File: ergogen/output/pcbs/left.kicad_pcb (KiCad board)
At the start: 2 copper layers, 122 x 109.6 mm, 29 parts

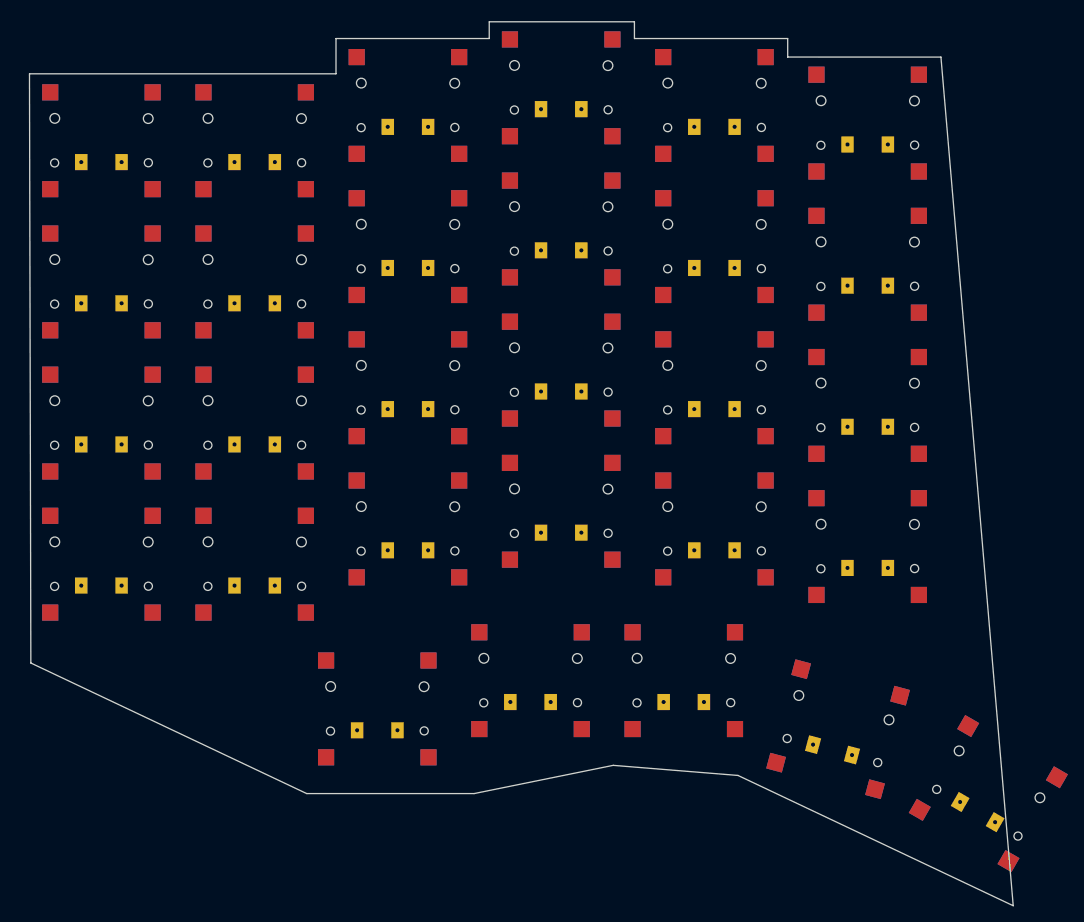
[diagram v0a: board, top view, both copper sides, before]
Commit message: feat: sane outline for left pcb
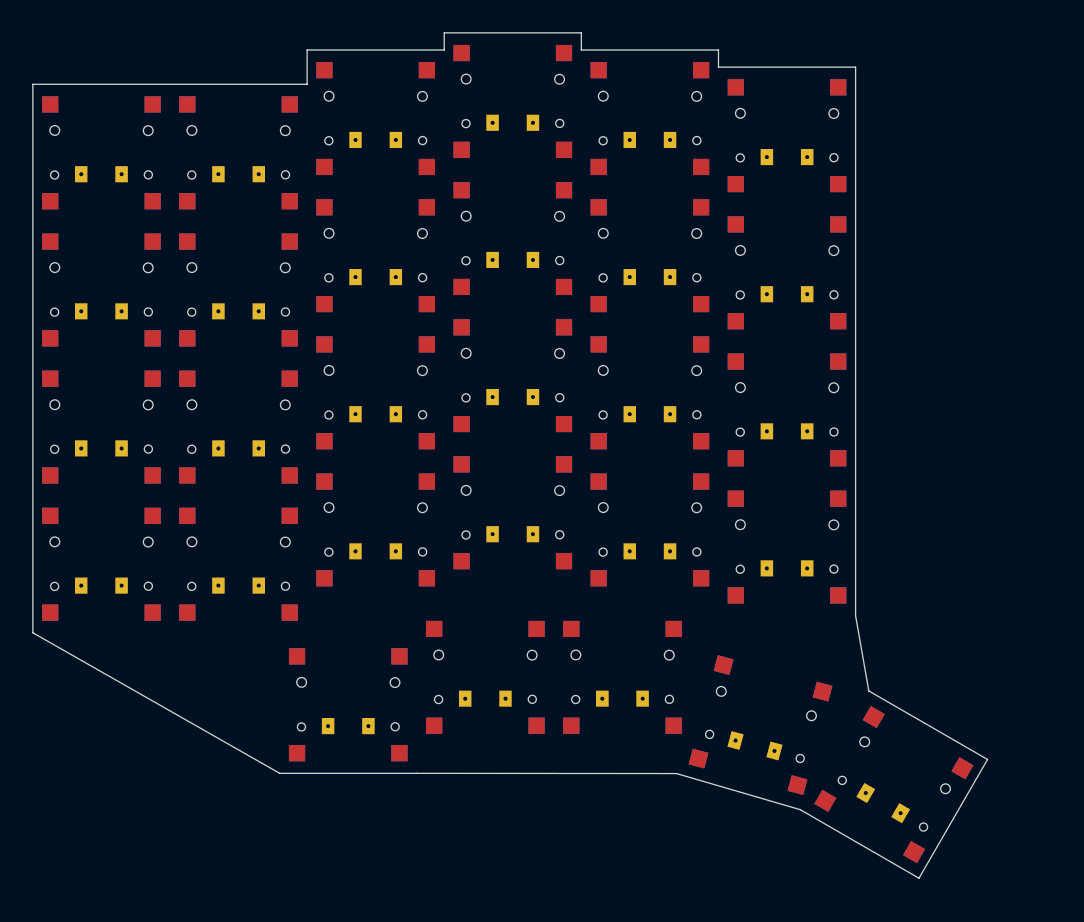
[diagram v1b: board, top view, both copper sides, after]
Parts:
- moved S29 11.8 mm to (198.2, 127.3)
- moved S24 10.1 mm to (185.0, 46.9)
- moved S23 10.1 mm to (185.0, 63.9)
- moved S22 10.0 mm to (185.0, 80.9)
- moved S21 10.0 mm to (185.0, 97.9)
- moved S28 9.63 mm to (181.7, 119.9)
- moved S20 8.16 mm to (168.0, 44.8)
- moved S19 8.08 mm to (168.0, 61.8)
- moved S18 8.02 mm to (168.0, 78.8)
- moved S17 8.00 mm to (168.0, 95.8)
- moved S27 7.61 mm to (164.6, 114.0)
- moved S16 6.23 mm to (151.0, 42.6)
- moved S15 6.12 mm to (151.0, 59.6)
- moved S14 6.04 mm to (151.0, 76.6)
- moved S13 6.00 mm to (151.0, 93.6)
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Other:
- board size 122 x 109.6 mm -> 118.4 x 104.8 mm
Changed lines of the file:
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@@
 )
 (footprint "CPG1316S01D02_reversible"
-(at 100 82.5 0)
+(at 100 83 0)
 (layer F.Cu)
 (attr smd)
@@
 )
 (footprint "CPG1316S01D02_reversible"
-(at 100 65 0)
+(at 100 66 0)
 (layer F.Cu)
 (attr smd)
@@
 )
 (footprint "CPG1316S01D02_reversible"
-(at 100 47.5 0)
+(at 100 49 0)
 (layer F.Cu)
 (attr smd)
@@
 )
 (footprint "CPG1316S01D02_reversible"
-(at 119 100 0)
+(at 117 100 0)
 (layer F.Cu)
 (attr smd)
@@
 )
 (footprint "CPG1316S01D02_reversible"
-(at 119 82.5 0)
+(at 117 83 0)
 (layer F.Cu)
 (attr smd)
@@
 )
 (footprint "CPG1316S01D02_reversible"
-(at 119 65 0)
+(at 117 66 0)
 (layer F.Cu)
 (attr smd)
@@
 )
 (footprint "CPG1316S01D02_reversible"
-(at 119 47.5 0)
+(at 117 49 0)
 (layer F.Cu)
 (attr smd)
@@
 )
 (footprint "CPG1316S01D02_reversible"
-(at 138 95.625 0)
+(at 134 95.75 0)
 (layer F.Cu)
 (attr smd)
@@
 )
 (footprint "CPG1316S01D02_reversible"
-(at 138 78.125 0)
+(at 134 78.75 0)
 (layer F.Cu)
 (attr smd)
@@
 )
 (footprint "CPG1316S01D02_reversible"
-(at 138 60.625 0)
+(at 134 61.75 0)
 (layer F.Cu)
 (attr smd)
@@
 )
 (footprint "CPG1316S01D02_reversible"
-(at 138 43.125 0)
+(at 134 44.75 0)
 (layer F.Cu)
 (attr smd)
@@
 )
 (footprint "CPG1316S01D02_reversible"
-(at 157 93.4375 0)
+(at 151 93.625 0)
 (layer F.Cu)
 (attr smd)
@@
 )
 (footprint "CPG1316S01D02_reversible"
-(at 157 75.9375 0)
+(at 151 76.625 0)
 (layer F.Cu)
 (attr smd)
@@
 )
 (footprint "CPG1316S01D02_reversible"
-(at 157 58.4375 0)
+(at 151 59.625 0)
 (layer F.Cu)
 (attr smd)
@@
 )
 (footprint "CPG1316S01D02_reversible"
-(at 157 40.9375 0)
+(at 151 42.625 0)
 (layer F.Cu)
 (attr smd)
@@
 )
 (footprint "CPG1316S01D02_reversible"
-(at 176 95.625 0)
+(at 168 95.75 0)
 (layer F.Cu)
 (attr smd)
@@
 )
 (footprint "CPG1316S01D02_reversible"
-(at 176 78.125 0)
+(at 168 78.75 0)
 (layer F.Cu)
 (attr smd)
@@
 )
 (footprint "CPG1316S01D02_reversible"
-(at 176 60.625 0)
+(at 168 61.75 0)
 (layer F.Cu)
 (attr smd)
@@
 )
 (footprint "CPG1316S01D02_reversible"
-(at 176 43.125 0)
+(at 168 44.75 0)
 (layer F.Cu)
 (attr smd)
@@
 )
 (footprint "CPG1316S01D02_reversible"
-(at 195 97.8125 0)
+(at 185 97.875 0)
 (layer F.Cu)
 (attr smd)
@@
 )
 (footprint "CPG1316S01D02_reversible"
-(at 195 80.3125 0)
+(at 185 80.875 0)
 (layer F.Cu)
 (attr smd)
@@
 )
 (footprint "CPG1316S01D02_reversible"
-(at 195 62.8125 0)
+(at 185 63.875 0)
 (layer F.Cu)
 (attr smd)
@@
 )
 (footprint "CPG1316S01D02_reversible"
-(at 195 45.3125 0)
+(at 185 46.875 0)
 (layer F.Cu)
 (attr smd)
@@
 )
 (footprint "CPG1316S01D02_reversible"
-(at 134.2 117.9375 0)
+(at 130.6 117.425 0)
 (layer F.Cu)
 (attr smd)
@@
 )
 (footprint "CPG1316S01D02_reversible"
-(at 153.2 114.4375 0)
+(at 147.6 114.025 0)
 (layer F.Cu)
 (attr smd)
@@
 )
 (footprint "CPG1316S01D02_reversible"
-(at 172.2 114.4375 0)
+(at 164.6 114.025 0)
 (layer F.Cu)
 (attr smd)
@@
 )
 (footprint "CPG1316S01D02_reversible"
-(at 191.3294819 120.4539876 -15)
+(at 181.7158522 119.9450152 -15)
 (layer F.Cu)
 (attr smd)
@@
 )
 (footprint "CPG1316S01D02_reversible"
-(at 209.9571424 128.4361508 -30)
+(at 198.2484958 127.3194102 -30)
 (layer F.Cu)
 (attr smd)
@@
 (model "models/PG1316S--装配体.STEP" (offset (xyz -4.75 -6.25 -10.25)) (scale (xyz 1 1 1)) (rotate (xyz 0 0 0)))
 )
-  (gr_line (start 91.25 112.25) (end 91.08 39.2025) (layer Edge.Cuts) (stroke (width 0.15) (type default)))
-(gr_line (start 91.08 39.2025) (end 129.08 39.2015) (layer Edge.Cuts) (stroke (width 0.15) (type default)))
-(gr_line (start 129.08 39.2015) (end 129.08 34.8275) (layer Edge.Cuts) (stroke (width 0.15) (type default)))
-(gr_line (start 129.08 34.8275) (end 148.08 34.8275) (layer Edge.Cuts) (stroke (width 0.15) (type default)))
-(gr_line (start 148.08 34.8275) (end 148.08 32.7525) (layer Edge.Cuts) (stroke (width 0.15) (type default)))
-(gr_line (start 148.08 32.7525) (end 166.082 32.7525) (layer Edge.Cuts) (stroke (width 0.15) (type default)))
-(gr_line (start 166.082 32.7525) (end 166.082 34.8275) (layer Edge.Cuts) (stroke (width 0.15) (type default)))
-(gr_line (start 166.082 34.8275) (end 185.082 34.8275) (layer Edge.Cuts) (stroke (width 0.15) (type default)))
-(gr_line (start 185.082 34.8275) (end 185.082 37.123) (layer Edge.Cuts) (stroke (width 0.15) (type default)))
-(gr_line (start 185.082 37.123) (end 204.082 37.1275) (layer Edge.Cuts) (stroke (width 0.15) (type default)))
-(gr_line (start 204.082 37.1275) (end 213.04263690000002 142.3419175) (layer Edge.Cuts) (stroke (width 0.15) (type default)))
-(gr_line (start 213.04263690000002 142.3419175) (end 178.9225941 126.1882386) (layer Edge.Cuts) (stroke (width 0.15) (type default)))
-(gr_line (start 178.9225941 126.1882386) (end 163.45 124.9375) (layer Edge.Cuts) (stroke (width 0.15) (type default)))
-(gr_line (start 163.45 124.9375) (end 146.2 128.4375) (layer Edge.Cuts) (stroke (width 0.15) (type default)))
-(gr_line (start 146.2 128.4375) (end 125.44999999999999 128.4375) (layer Edge.Cuts) (stroke (width 0.15) (type default)))
-(gr_line (start 125.44999999999999 128.4375) (end 91.25 112.25) (layer Edge.Cuts) (stroke (width 0.15) (type default)))
-)
+  (gr_line (start 91.5 108.5) (end 91.5 40.5) (layer Edge.Cuts) (stroke (width 0.15) (type default)))
+(gr_line (start 91.5 40.5) (end 125.5 40.5) (layer Edge.Cuts) (stroke (width 0.15) (type default)))
+(gr_line (start 125.5 40.5) (end 125.5 36.25) (layer Edge.Cuts) (stroke (width 0.15) (type default)))
+(gr_line (start 125.5 36.25) (end 142.5 36.25) (layer Edge.Cuts) (stroke (width 0.15) (type default)))
+(gr_line (start 142.5 36.25) (end 142.5 34.125) (layer Edge.Cuts) (stroke (width 0.15) (type default)))
+(gr_line (start 142.5 34.125) (end 159.5 34.125) (layer Edge.Cuts) (stroke (width 0.15) (type default)))
+(gr_line (start 159.5 34.125) (end 159.5 36.25) (layer Edge.Cuts) (stroke (width 0.15) (type default)))
+(gr_line (start 159.5 36.25) (end 176.5 36.25) (layer Edge.Cuts) (stroke (width 0.15) (type default)))
+(gr_line (start 176.5 36.25) (end 176.5 38.375) (layer Edge.Cuts) (stroke (width 0.15) (type default)))
+(gr_line (start 176.5 38.375) (end 193.5 38.375) (layer Edge.Cuts) (stroke (width 0.15) (type default)))
+(gr_line (start 193.5 38.375) (end 193.5 106.375) (layer Edge.Cuts) (stroke (width 0.15) (type default)))
+(gr_line (start 193.5 106.375) (end 195.1372799 115.70819429999999) (layer Edge.Cuts) (stroke (width 0.15) (type default)))
+(gr_line (start 195.1372799 115.70819429999999) (end 209.8597117 124.20819429999999) (layer Edge.Cuts) (stroke (width 0.15) (type default)))
+(gr_line (start 209.8597117 124.20819429999999) (end 201.3597117 138.93062609999998) (layer Edge.Cuts) (stroke (width 0.15) (type default)))
+(gr_line (start 201.3597117 138.93062609999998) (end 186.6372799 130.43062609999998) (layer Edge.Cuts) (stroke (width 0.15) (type default)))
+(gr_line (start 186.6372799 130.43062609999998) (end 171.3055208 125.9554228) (layer Edge.Cuts) (stroke (width 0.15) (type default)))
+(gr_line (start 171.3055208 125.9554228) (end 139.1 125.925) (layer Edge.Cuts) (stroke (width 0.15) (type default)))
+(gr_line (start 139.1 125.925) (end 122.1 125.925) (layer Edge.Cuts) (stroke (width 0.15) (type default)))
+(gr_line (start 122.1 125.925) (end 91.5 108.5) (layer Edge.Cuts) (stroke (width 0.15) (type default)))
+)

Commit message: feat: improved ergogen component names in general
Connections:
- net big_outward_home renamed thumbkey_home
- net extra_outward_home renamed small_thumbkey_home
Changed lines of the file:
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@@
 (net 32 "mid_home")
 (net 33 "outward_home")
-(net 34 "extra_outward_home")
-(net 35 "big_outward_home")
+(net 34 "small_thumbkey_home")
+(net 35 "thumbkey_home")
   (footprint "CPG1316S01D02_reversible"
 (at 100 100 0)
@@
 (property "Reference" "S28" hide (at 0 0 -15) (layer "F.SilkS") (effects (font (size 1 1) (thickness 0.15))))
 (pad "1" thru_hole rect (at -2.5 2.65 -15) (size 1.55 2) (drill 0.5) (layers "*.Cu" "*.Mask") (remove_unused_layers no) (thermal_bridge_angle 45) (net 21 "C4"))
-(pad "2" thru_hole rect (at 2.5 2.65 -15) (size 1.55 2) (drill 0.5) (layers "*.Cu" "*.Mask") (remove_unused_layers no) (thermal_bridge_angle 45) (net 34 "extra_outward_home"))
+(pad "2" thru_hole rect (at 2.5 2.65 -15) (size 1.55 2) (drill 0.5) (layers "*.Cu" "*.Mask") (remove_unused_layers no) (thermal_bridge_angle 45) (net 34 "small_thumbkey_home"))
 (pad "3" smd rect (at -6.35 -6 -15) (size 2 2) (layers "F.Cu" "F.Paste" "F.Mask") (thermal_bridge_angle 45) (net 0 ""))
 (pad "3" smd rect (at -6.35 -6 -15) (size 2 2) (layers "B.Cu" "B.Paste" "B.Mask") (thermal_bridge_angle 45) (net 0 ""))
@@
 (property "Reference" "S29" hide (at 0 0 -30) (layer "F.SilkS") (effects (font (size 1 1) (thickness 0.15))))
 (pad "1" thru_hole rect (at -2.5 2.65 -30) (size 1.55 2) (drill 0.5) (layers "*.Cu" "*.Mask") (remove_unused_layers no) (thermal_bridge_angle 45) (net 26 "C5"))
-(pad "2" thru_hole rect (at 2.5 2.65 -30) (size 1.55 2) (drill 0.5) (layers "*.Cu" "*.Mask") (remove_unused_layers no) (thermal_bridge_angle 45) (net 35 "big_outward_home"))
+(pad "2" thru_hole rect (at 2.5 2.65 -30) (size 1.55 2) (drill 0.5) (layers "*.Cu" "*.Mask") (remove_unused_layers no) (thermal_bridge_angle 45) (net 35 "thumbkey_home"))
 (pad "3" smd rect (at -6.35 -6 -30) (size 2 2) (layers "F.Cu" "F.Paste" "F.Mask") (thermal_bridge_angle 45) (net 0 ""))
 (pad "3" smd rect (at -6.35 -6 -30) (size 2 2) (layers "B.Cu" "B.Paste" "B.Mask") (thermal_bridge_angle 45) (net 0 ""))
